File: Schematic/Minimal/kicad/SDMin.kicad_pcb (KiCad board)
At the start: 4 copper layers, 75 x 135 mm, 89 parts, among them CON1 uSD_Card, P1 USB_B, P2 CONN_01X04, P3 CONN_01X04, P4 CONN_01X04, P5 CONN_01X03, P6 CONN_01X02, SW1 SW_PUSH, SW2 SW_PUSH, SW3 SW_PUSH, SW4 SW_PUSH, SW5 SW_PUSH, SW6 SW_PUSH, SW7 SW_PUSH, SW8 SW_PUSH, SW9 SW_PUSH, U1 PAM2301, U10 ADMP401-BB, U11 RN-52, U12 STA013, U2 XC9140, U3 MCP73811/2, U4 STM32L476R, U5 Lightware_SF10/A, U6 UART, U7 DebugPins, U8 MLX90393, U9 LS20031, X1 14.7456MHz

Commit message: PCB svg render
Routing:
- net /in6: track 0.00 -> 154.2 mm, vias 0 -> 1
- net /in1: track 0.00 -> 137.0 mm
- net GND: track 0.00 -> 134.5 mm, vias 0 -> 50
- net /in7: track 0.00 -> 131.9 mm
- net /in8: track 0.00 -> 126.0 mm, vias 0 -> 1
- net PB7_GPS-TX: track 0.00 -> 125.0 mm, vias 0 -> 1
- net /in3: track 0.00 -> 117.0 mm
- net +3V3: track 0.00 -> 112.0 mm, vias 0 -> 32
- net /in4: track 0.00 -> 107.5 mm
- net +5V: track 0.00 -> 106.2 mm
- net /5VEN: track 0.00 -> 102.0 mm, vias 0 -> 2
- net /in5: track 0.00 -> 95.5 mm, vias 0 -> 1
- net PC8_SD-D0: track 0.00 -> 91.2 mm, vias 0 -> 2
- net /in2: track 0.00 -> 90.9 mm, vias 0 -> 1
- net PC11_SD-D3: track 0.00 -> 87.1 mm, vias 0 -> 2
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
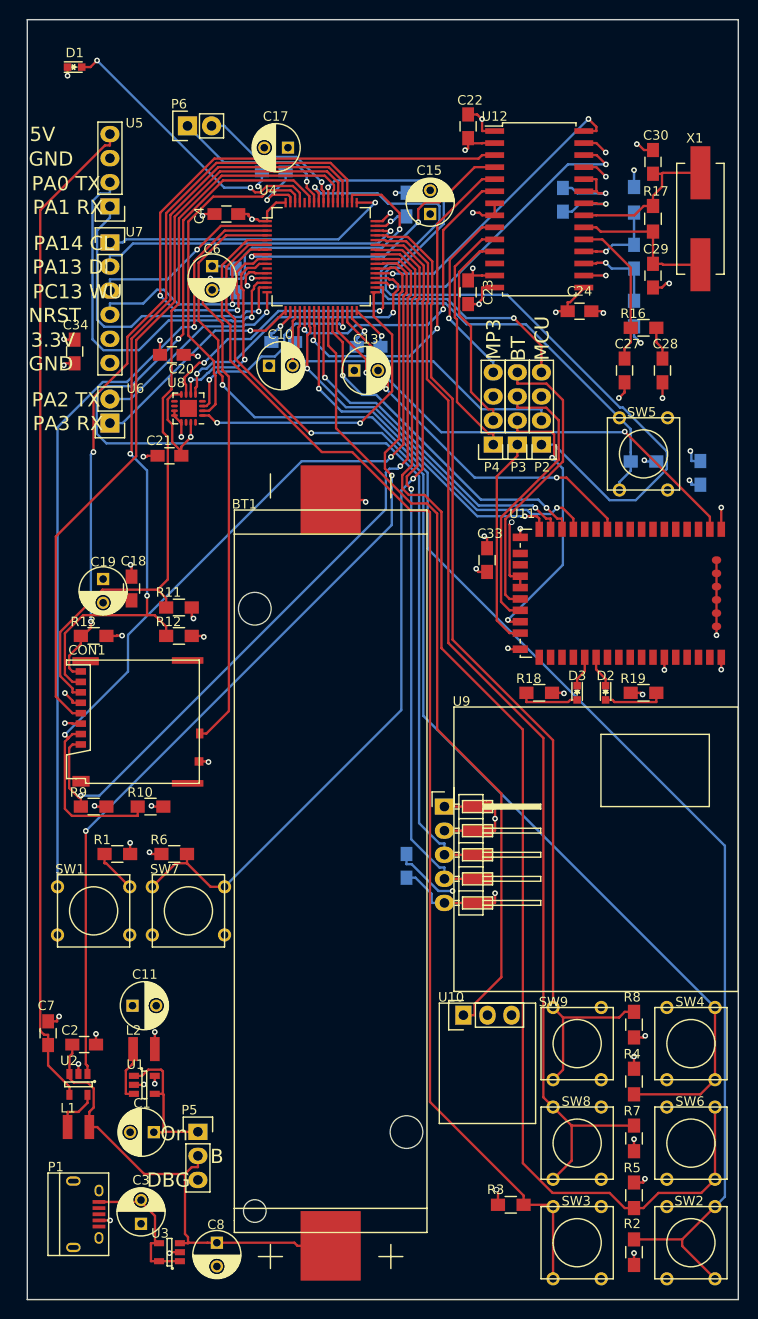
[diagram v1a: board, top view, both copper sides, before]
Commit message: Ordered PCB. Making no progress on the compass.
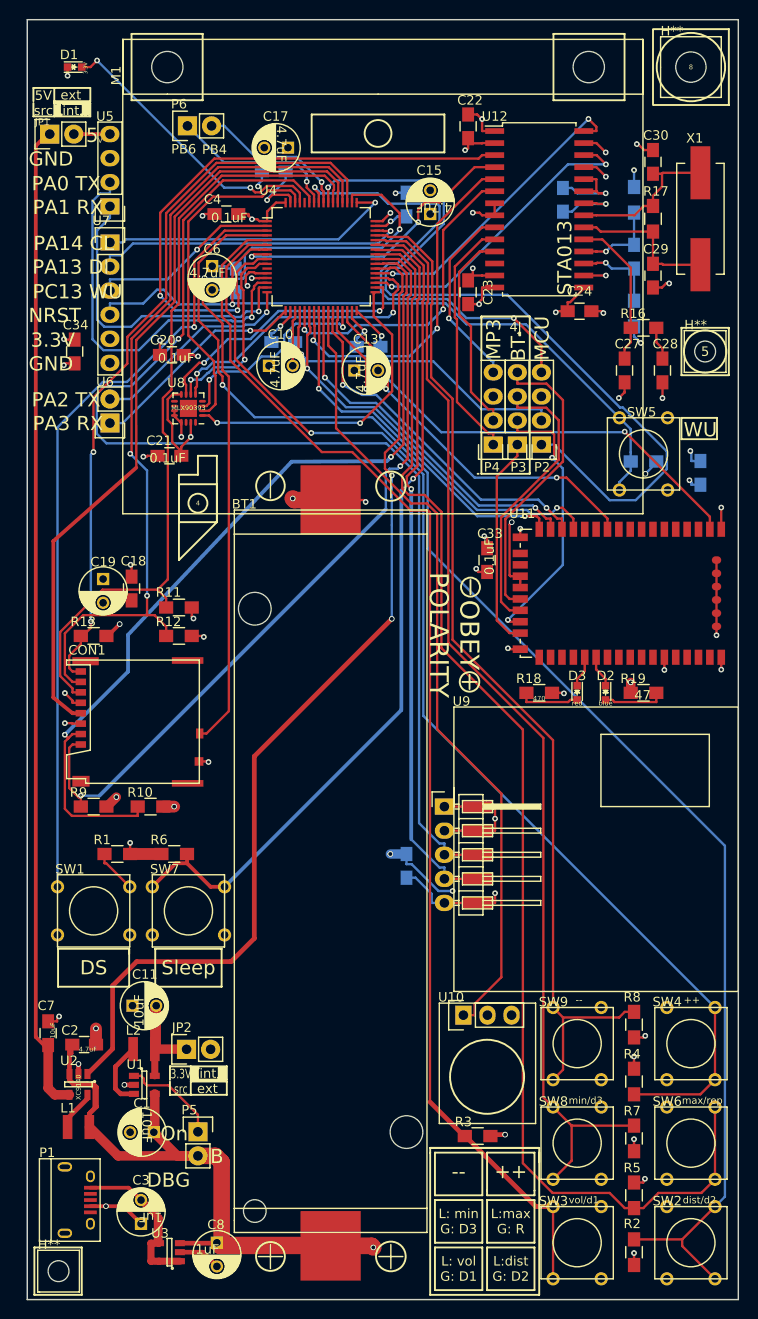
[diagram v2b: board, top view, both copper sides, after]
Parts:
- added H**: H2.2, con-trougnouf:mountinghole2.2, F.Cu at (40.3, 172.0)
- added H**: 3.2H, con-trougnouf:mountinghole3.2, F.Cu at (107.0, 45.0)
- added H**: H2.2, con-trougnouf:mountinghole2.2, F.Cu at (108.5, 75.0)
- added JP1: Jumper_NC_Small, Pin_Headers:Pin_Header_Straight_1x02, F.Cu at (39.4, 52.1)
- added JP2: Jumper_NC_Small, Pin_Headers:Pin_Header_Straight_1x02, F.Cu at (53.8, 148.6)
- added M1: LaserBracket, con-trougnouf:LaserHolder, F.Cu at (74.0, 45.0)
- P5: value CONN_01X03 -> CONN_01X02; footprint Pin_Headers:Pin_Header_Straight_1x03 -> Pin_Headers:Pin_Header_Straight_1x02
- moved R3 8.05 mm to (84.5, 157.8), turned to 180 degrees
- moved P1 1.75 mm to (42.1, 164.5)
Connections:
- C1 pad 1: /3VEN -> +BATT
- C11 pad 2: +3V3 -> Net-(C11-Pad2)
- C7 pad 1: +5V -> Net-(C7-Pad1)
- L2 pad 2: +3V3 -> Net-(C11-Pad2)
- U1 pad 4: /3VEN -> +BATT
- U1 pad 5: +3V3 -> Net-(C11-Pad2)
- U11 pad 39: GND -> (no net)
- U2 pad 4: +5V -> Net-(C7-Pad1)
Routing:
- net Net-(C7-Pad1): track 0.00 -> 104.6 mm
- net +5V: track 106.2 -> 3.81 mm
- net +BATT: track 49.4 -> 105.1 mm, vias 0 -> 1
- net Net-(C11-Pad2): track 0.00 -> 16.3 mm
- net GND: track 134.5 -> 149.8 mm, vias 50 -> 49
- net Net-(C3-Pad2): track 15.4 -> 26.1 mm
- net /5VEN: track 102.0 -> 107.7 mm
- net /3VEN: track 15.3 -> 10.5 mm
- net +3V3: track 112.0 -> 109.9 mm, vias 32 -> 30
- net PB2_BT-GP2: track 51.8 -> 53.6 mm
- net (no net): track 0.00 -> 1.34 mm, vias 0 -> 1
- net Net-(L2-Pad1): track 5.95 -> 7.12 mm
- net Net-(L1-Pad2): track 4.94 -> 4.27 mm
- net PC12_SD-CK: track 81.0 -> 81.7 mm
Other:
- board text added: "++"
- board text added: "--"
- board text added: "0.1uF"
- board text added: "10uF"
- board text added: "1uF"
- board text added: "3.3V src"
- board text added: "4"
- board text added: "4.7uF"
- board text added: "47"
- board text added: "470"
- board text added: "4J"
- board text added: "5"
- board text added: "5V src"
- board text added: "8"
- board text added: "DS"
- board text added: "L: min G: D3"
- board text added: "L: vol G: D1"
- board text added: "L:dist G: D2"
- board text added: "L:max G: R"
- board text added: "MLX90393"
- board text added: "OBEY POLARITY"
- board text added: "PB4"
- board text added: "PB6"
- board text added: "STA013"
- board text added: "Sensewalk 9000"
- board text added: "Sleep"
- board text added: "V"
- board text added: "WU"
- board text added: "XC9140"
- board text added: "blue"
- board text added: "dist/d2"
- board text added: "ext"
- board text added: "int"
- board text added: "max/rep"
- board text added: "min/d3"
- board text added: "red"
- board text added: "trougnouf"
- board text added: "vol/d1"
- board text removed: "5V"
